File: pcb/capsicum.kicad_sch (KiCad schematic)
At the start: 52 parts, among them J1 USB4510-03-1-A_REVA, J2 Screw_Terminal_01x02, Q1 BSS83P, Q2 BC817-16LT3G, SW1 SW_SPDT, SW3 SW_SPDT, U1 ESP32-C3-WROOM-02, U3 AP2112K, U4 MCP73831-2-OT

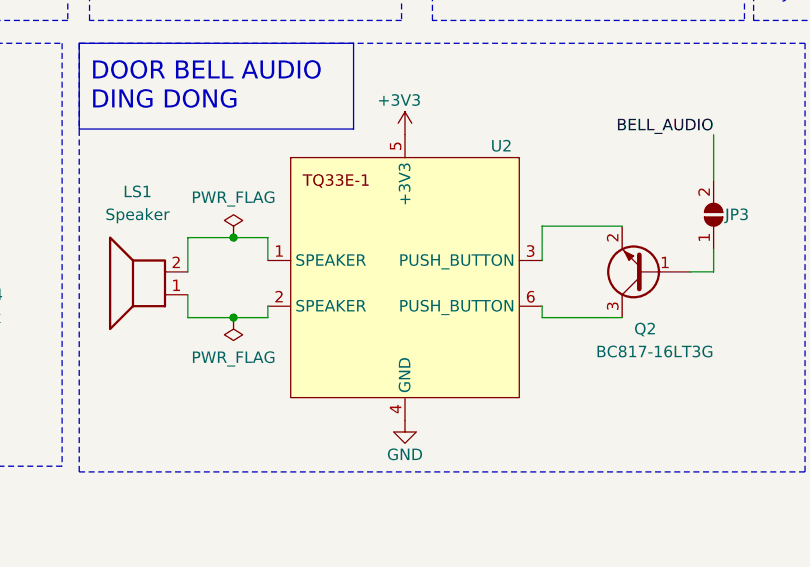
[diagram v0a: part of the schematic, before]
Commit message: feat: associate screw terminal part
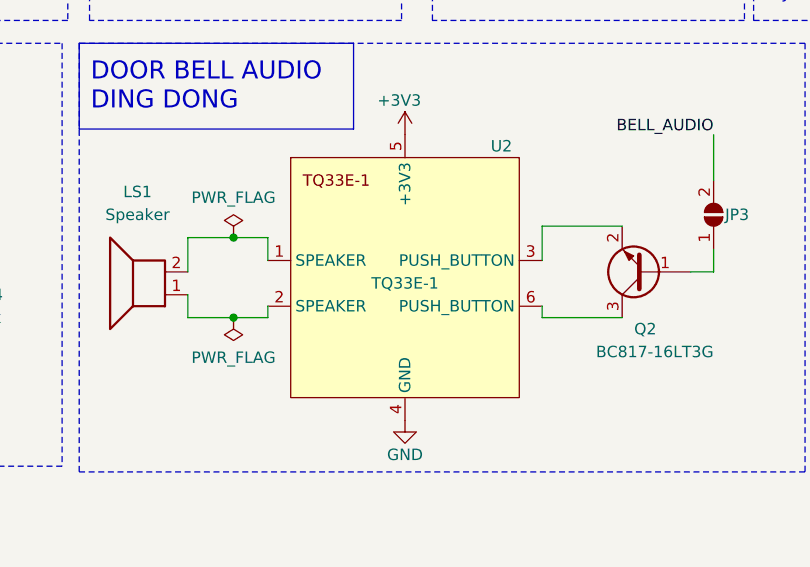
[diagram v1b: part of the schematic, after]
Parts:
- J2: footprint (none) -> Screw Terminal:phoenix_screw_terminal_th_1935161; Link (none) -> https://www.pcbway.com/components/detail/1935161/483076/; MANUFACTURER (none) -> Phoenix; MPN (none) -> 1935161; Package (none) -> TH; SNAPEDA_PN (none) -> 1935161; Vendor (none) -> PCBWay
- TP1, TP2, TP3: footprint (none) -> TestPoint:TestPoint_Pad_1.5x1.5mm
- U2: value ~ -> TQ33E-1
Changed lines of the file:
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@@
       (effects (font (size 1.27 1.27)) (justify right) hide)
     )
-    (property "Footprint" "" (at 115.57 33.02 0)
+    (property "Footprint" "TestPoint:TestPoint_Pad_1.5x1.5mm" (at 115.57 33.02 0)
       (effects (font (size 1.27 1.27)) hide)
     )
@@
       (effects (font (size 1.27 1.27)) (justify right) hide)
     )
-    (property "Footprint" "" (at 68.58 35.56 0)
+    (property "Footprint" "TestPoint:TestPoint_Pad_1.5x1.5mm" (at 68.58 35.56 0)
       (effects (font (size 1.27 1.27)) hide)
     )
@@
       (effects (font (size 1.27 1.27)))
     )
-    (property "Footprint" "" (at 25.4 175.26 0)
-      (effects (font (size 1.27 1.27)) hide)
-    )
-    (property "Datasheet" "~" (at 25.4 175.26 0)
-      (effects (font (size 1.27 1.27)) hide)
-    )
-    (property "MPN" "" (at 25.4 175.26 0)
-      (effects (font (size 1.27 1.27)) hide)
-    )
-    (property "Package" "" (at 25.4 175.26 0)
+    (property "Footprint" "Screw Terminal:phoenix_screw_terminal_th_1935161" (at 25.4 175.26 0)
+      (effects (font (size 1.27 1.27)) hide)
+    )
+    (property "Datasheet" "https://media.digikey.com/pdf/Data%20Sheets/Phoenix%20Contact%20PDFs/1935161.pdf" (at 25.4 175.26 0)
+      (effects (font (size 1.27 1.27)) hide)
+    )
+    (property "MPN" "1935161" (at 25.4 175.26 0)
+      (effects (font (size 1.27 1.27)) hide)
+    )
+    (property "Package" "TH" (at 25.4 175.26 0)
+      (effects (font (size 1.27 1.27)) hide)
+    )
+    (property "Link" "https://www.pcbway.com/components/detail/1935161/483076/" (at 25.4 175.26 0)
+      (effects (font (size 1.27 1.27)) hide)
+    )
+    (property "MANUFACTURER" "Phoenix" (at 25.4 175.26 0)
+      (effects (font (size 1.27 1.27)) hide)
+    )
+    (property "SNAPEDA_PN" "1935161" (at 25.4 175.26 0)
+      (effects (font (size 1.27 1.27)) hide)
+    )
+    (property "Vendor" "PCBWay" (at 25.4 175.26 0)
       (effects (font (size 1.27 1.27)) hide)
     )
@@
       (effects (font (size 1.27 1.27)) (justify right) hide)
     )
-    (property "Footprint" "" (at 162.56 67.31 0)
+    (property "Footprint" "TestPoint:TestPoint_Pad_1.5x1.5mm" (at 162.56 67.31 0)
       (effects (font (size 1.27 1.27)) hide)
     )
@@
       (effects (font (size 1.27 1.27)) (justify left))
     )
-    (property "Value" "~" (at 207.01 113.03 0)
+    (property "Value" "TQ33E-1" (at 207.01 113.03 0)
       (effects (font (size 1.27 1.27)))
     )
@@
       (effects (font (size 1.27 1.27)) hide)
     )
-    (property "Datasheet" "" (at 207.01 113.03 0)
-      (effects (font (size 1.27 1.27)) hide)
-    )
+    (property "Datasheet" "https://www.yoycart.com/Product/550682313846/" (at 207.01 113.03 0)
+      (effects (font (size 1.27 1.27)) hide)
+    )

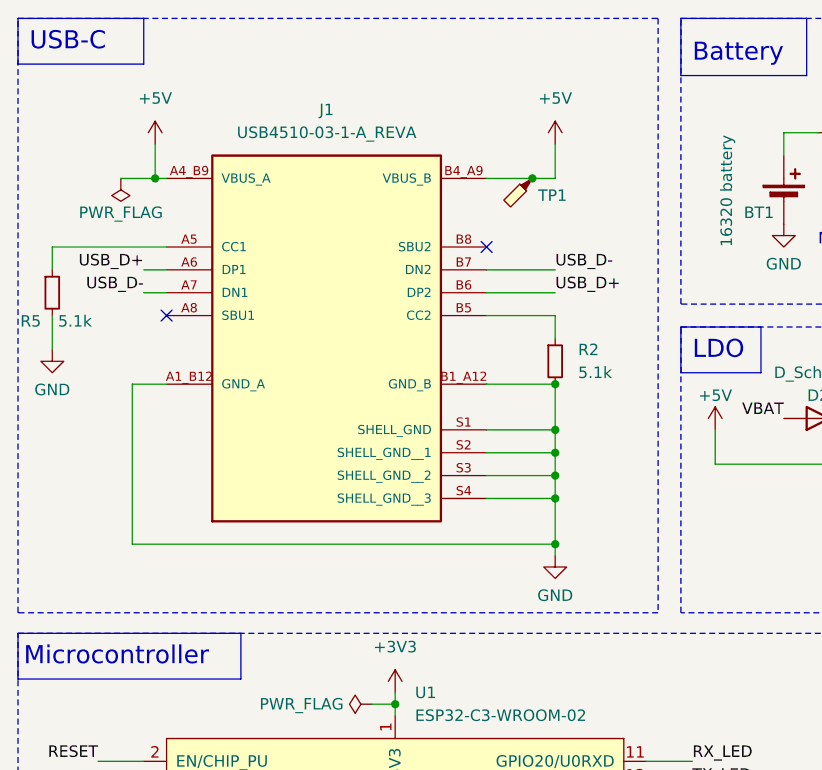
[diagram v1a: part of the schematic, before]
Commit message: feat: associate USB-C through-hole 16+8 USB2.0 connector footprint
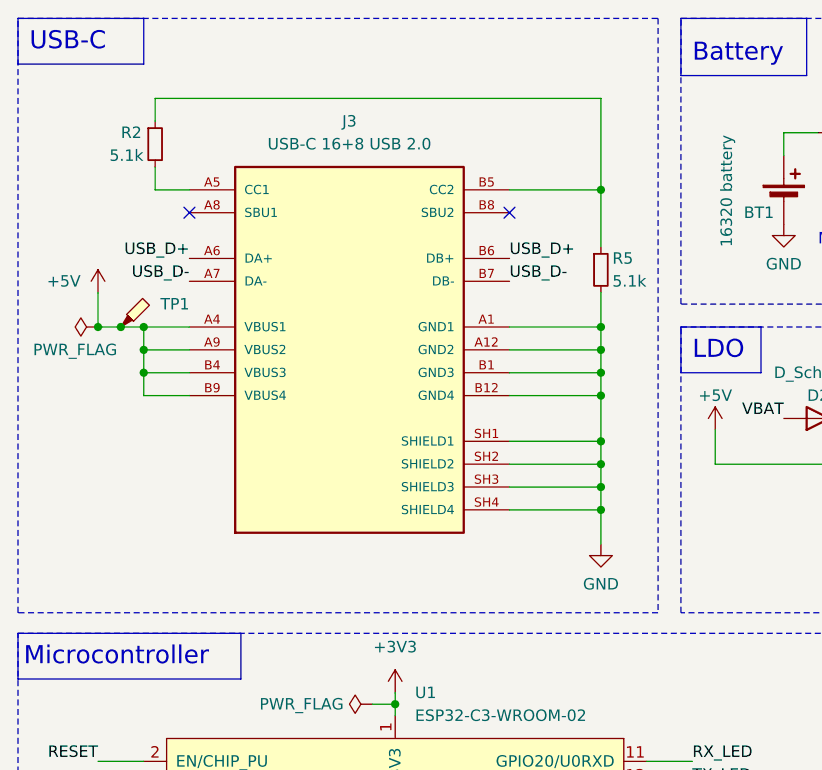
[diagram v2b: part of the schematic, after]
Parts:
- removed J1: USB4510-03-1-A_REVA, GCT_USB_C:GCT_USB4510-03-1-A_REVA, symbol GCT_USB_C:USB4510-03-1-A_REVA
- added J3: USB-C 16+8 USB 2.0, Molex_USB_C:Molex_USB_C_2137160001, symbol Molex_USB_C:2137160001
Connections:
- net +5V: now also J3.A4 (VBUS1), J3.A9 (VBUS2), J3.B4 (VBUS3), J3.B9 (VBUS4)
- net GND: now also J3.A1 (GND1), J3.A12 (GND2), J3.B1 (GND3), J3.B12 (GND4), J3.SH1 (SHIELD1), J3.SH2 (SHIELD2), J3.SH3 (SHIELD3), J3.SH4 (SHIELD4); no longer R2.2
- net USB_D+: now also J3.A6 (DA+), J3.B6 (DB+)
- net USB_D-: now also J3.A7 (DA-), J3.B7 (DB-)
- net at R5.1: now also R2.1, J3.B5 (CC2)
- new net: J3.A5 (CC1), R2.2
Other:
- moved on the sheet: R2, R5, TP1

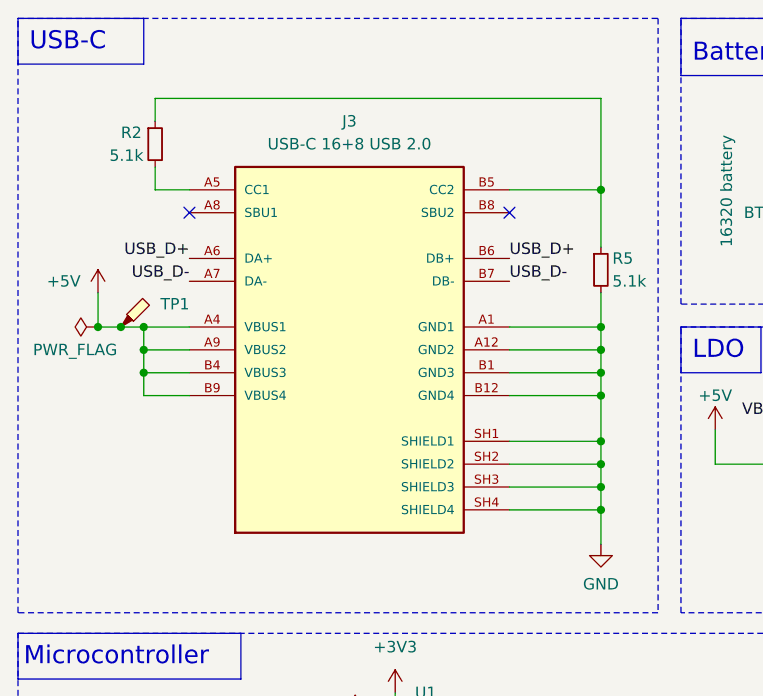
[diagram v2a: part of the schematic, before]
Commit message: feat: add resistors to combined D+ D-
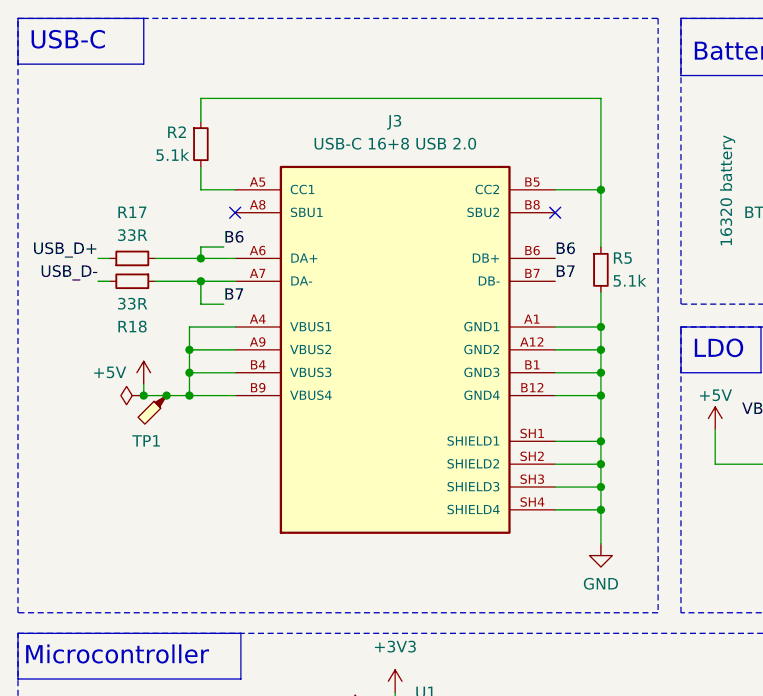
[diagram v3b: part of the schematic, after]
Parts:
- added R17, R18: 33R, symbol Device:R_Small
- Q2: footprint Package_TO_SOT_SMD:SOT-23 -> Package_TO_SOT_SMD:SOT-23-3; Package (none) -> SOT-23-3
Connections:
- net USB_D+: now also R17.1; no longer J3.A6 (DA+), J3.B6 (DB+)
- net USB_D-: now also R18.2; no longer J3.A7 (DA-), J3.B7 (DB-)
- new net B6: J3.A6 (DA+), J3.B6 (DB+), R17.2
- new net B7: J3.A7 (DA-), J3.B7 (DB-), R18.1
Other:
- moved on the sheet: J3, R2, TP1

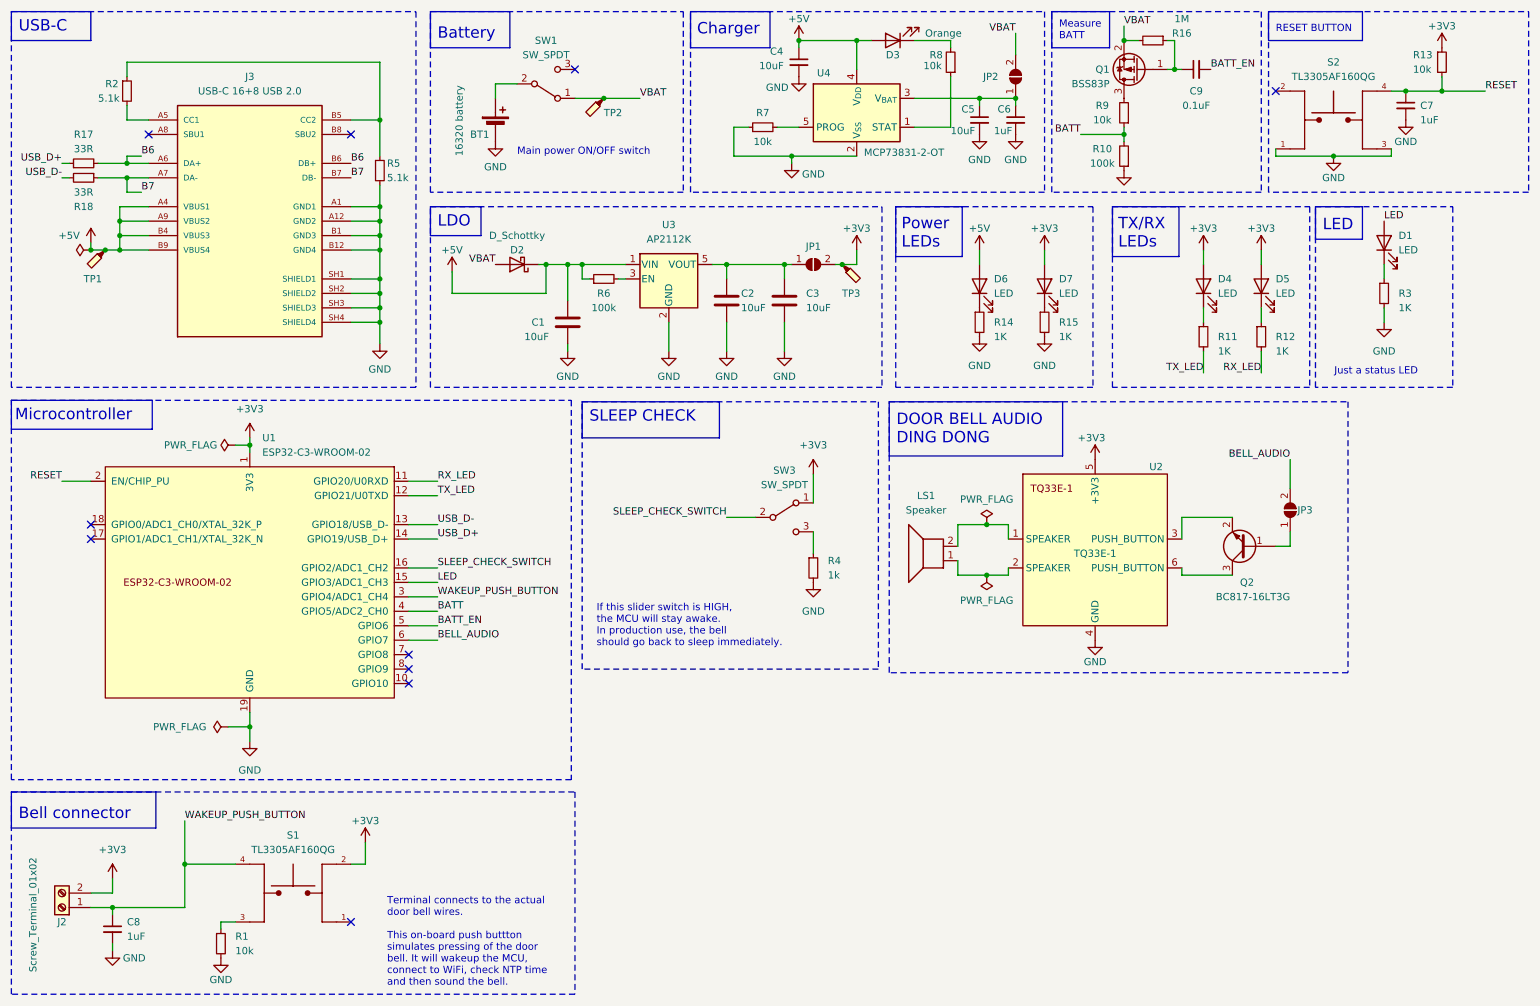
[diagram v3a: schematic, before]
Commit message: feat: add test points and bridged jumpers
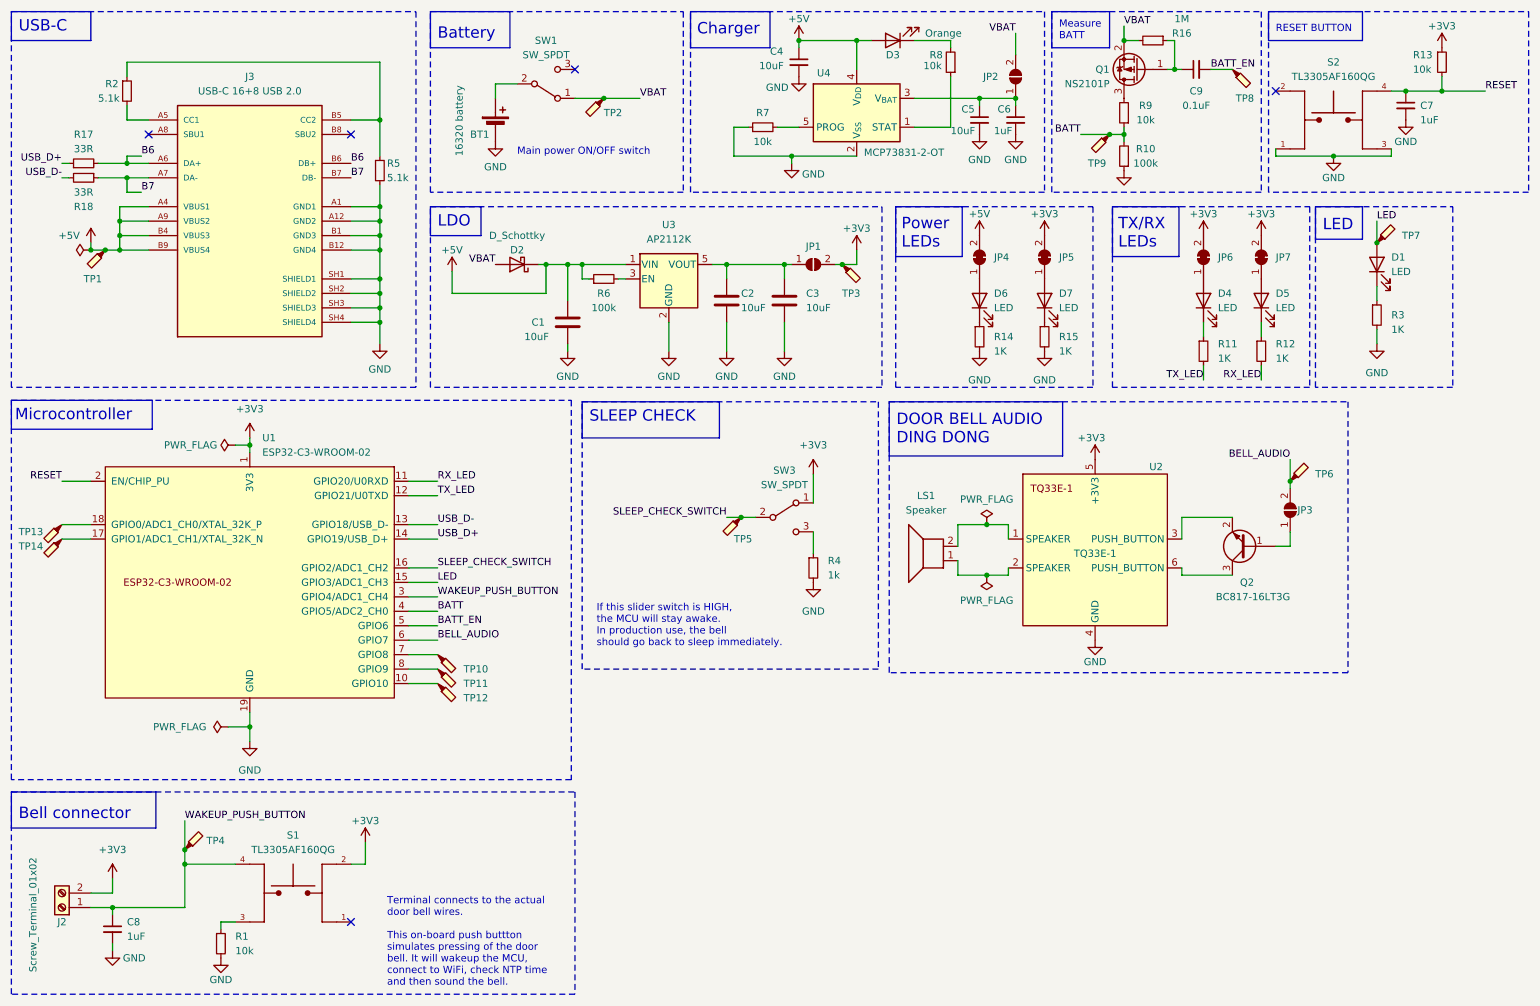
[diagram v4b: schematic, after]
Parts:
- added JP4, JP5, JP6, JP7: SolderJumper_2_Bridged, Jumper:SolderJumper-2_P1.3mm_Bridged_RoundedPad1.0x1.5mm, symbol Jumper:SolderJumper_2_Bridged
- added TP10, TP11, TP12, TP13, TP14, TP4, TP5, TP6, TP7, TP8, TP9: TestPoint_Probe, TestPoint:TestPoint_Pad_1.5x1.5mm, symbol Connector:TestPoint_Probe
- C9: footprint (none) -> Capacitor_SMD:C_0603_1608Metric
- JP1, JP2, JP3, LS1: footprint (none) -> Jumper:SolderJumper-2_P1.3mm_Open_RoundedPad1.0x1.5mm
- Q1: value BSS83P -> NS2101P
- R17, R18: footprint (none) -> Resistor_SMD:R_0603_1608Metric
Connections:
- net +3V3: now also JP5.2 (B), JP6.2 (B), JP7.2 (B); no longer D4.2 (A), D5.2 (A), D7.2 (A)
- net +5V: now also JP4.2 (B); no longer D6.2 (A)
- net BATT: now also TP9.1
- net BATT_EN: now also TP8.1
- net BELL_AUDIO: now also TP6.1
- net LED: now also TP7.1
- net SLEEP_CHECK_SWITCH: now also TP5.1
- net WAKEUP_PUSH_BUTTON: now also TP4.1
- net at U1.10 (GPIO10): now also TP12.1
- net at U1.17 (GPIO1/ADC1_CH1/XTAL_32K_N): now also TP14.1
- net at U1.18 (GPIO0/ADC1_CH0/XTAL_32K_P): now also TP13.1
- net at U1.7 (GPIO8): now also TP10.1
- net at U1.8 (GPIO9): now also TP11.1
- new net: D5.2 (A), JP7.1 (A)
- new net: D6.2 (A), JP4.1 (A)
- new net: D7.2 (A), JP5.1 (A)
- new net: D4.2 (A), JP6.1 (A)
- no-connect marks 10 -> 5
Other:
- note removed: "Just a status LED"
- moved on the sheet: D1, D4, D5, D6, D7, R11, R12, R14, R15, R3

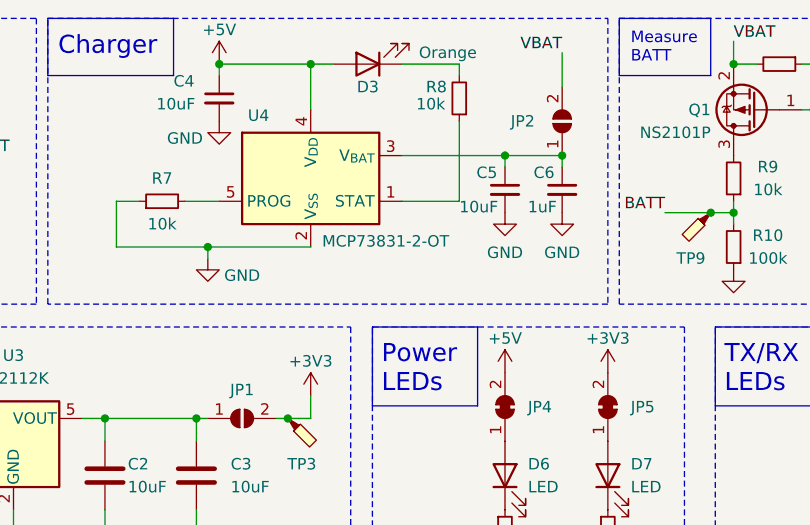
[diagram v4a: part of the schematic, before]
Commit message: feat: associate MPN and BOM details to battery monitoring circuit MOSFET
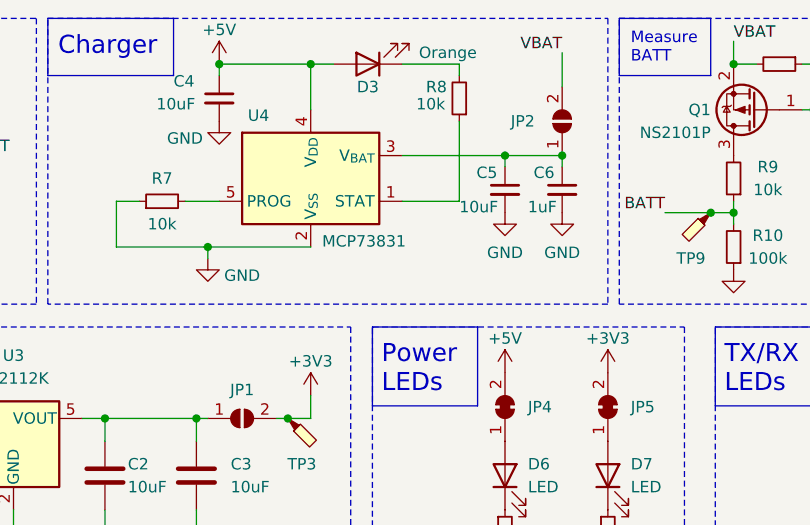
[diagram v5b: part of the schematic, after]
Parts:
- Q1: footprint Package_TO_SOT_SMD:SOT-23 -> Package_TO_SOT_SMD:SOT-323_SC-70; Link (none) -> https://www.pcbway.com/components/detail/NTS2101PT1G/343596/; MANUFACTURER (none) -> OnSemi; MPN (none) -> NTS2101PT1G; Package (none) -> SC-70-3 (SOT323); Vendor (none) -> PCBWay
- U4: value MCP73831-2-OT -> MCP73831
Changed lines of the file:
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@@
       (effects (font (size 1.27 1.27)) (justify left))
     )
-    (property "Footprint" "Package_TO_SOT_SMD:SOT-23" (at 209.55 26.035 0)
+    (property "Footprint" "Package_TO_SOT_SMD:SOT-323_SC-70" (at 209.55 26.035 0)
       (effects (font (size 1.27 1.27) italic) (justify left) hide)
     )
@@
       (effects (font (size 1.27 1.27)) (justify left) hide)
     )
-    (property "Package" "" (at 214.63 27.94 0)
+    (property "Package" "SC-70-3 (SOT323)" (at 214.63 27.94 0)
+      (effects (font (size 1.27 1.27)) hide)
+    )
+    (property "Link" "https://www.pcbway.com/components/detail/NTS2101PT1G/343596/" (at 214.63 27.94 0)
+      (effects (font (size 1.27 1.27)) hide)
+    )
+    (property "MANUFACTURER" "OnSemi" (at 214.63 27.94 0)
+      (effects (font (size 1.27 1.27)) hide)
+    )
+    (property "MPN" "NTS2101PT1G" (at 214.63 27.94 0)
+      (effects (font (size 1.27 1.27)) hide)
+    )
+    (property "Vendor" "PCBWay" (at 214.63 27.94 0)
       (effects (font (size 1.27 1.27)) hide)
     )
@@
       (effects (font (size 1.27 1.27)) (justify left))
     )
-    (property "Value" "MCP73831-2-OT" (at 166.37 42.545 0)
-      (effects (font (size 1.27 1.27)) (justify left))
-    )
+    (property "Value" "MCP73831" (at 166.37 42.545 0)
+      (effects (font (size 1.27 1.27)) (justify left))
+    )
